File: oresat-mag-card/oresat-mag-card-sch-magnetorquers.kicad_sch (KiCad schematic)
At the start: 79 parts, among them U12 STSPIN250, U13 STSPIN250, U14 INA185, U15 INA185, U16 STSPIN250, U17 INA185

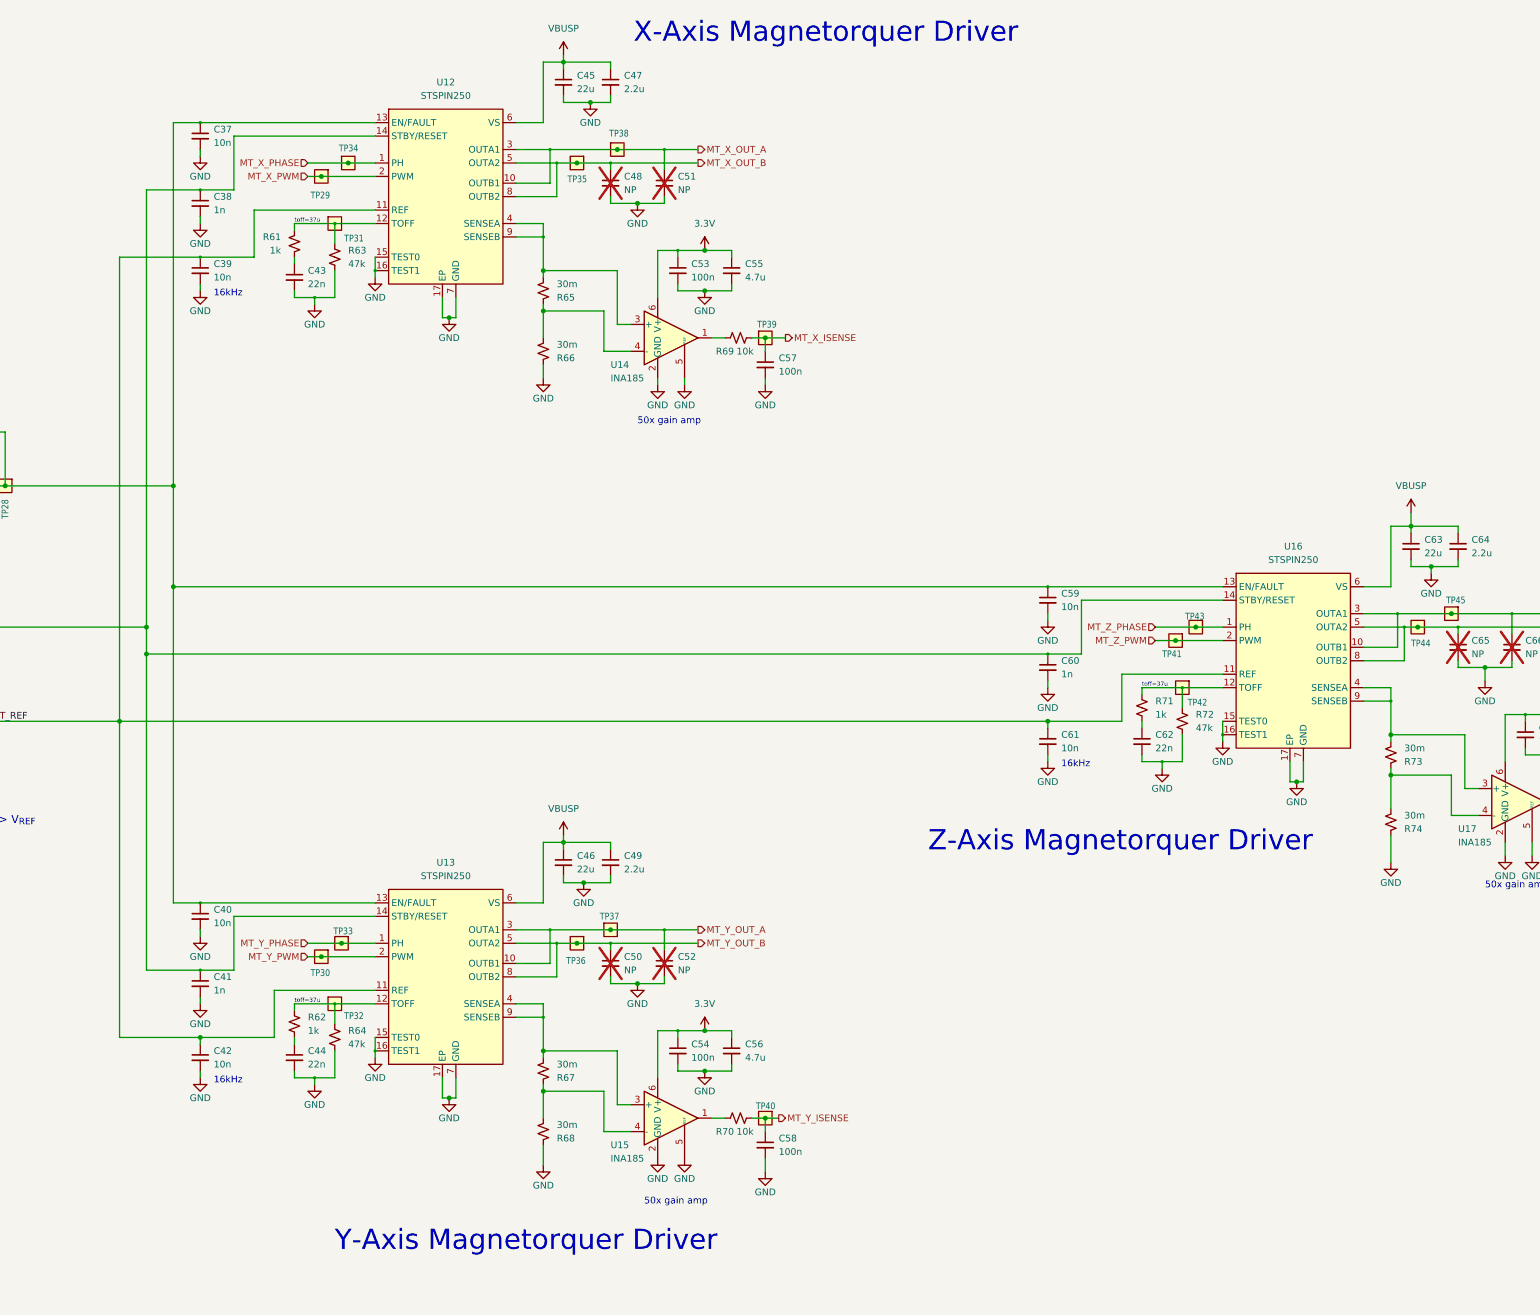
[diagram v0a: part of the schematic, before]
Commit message: Schematic polish, fixed UART TX/RX mixup, imported into layout
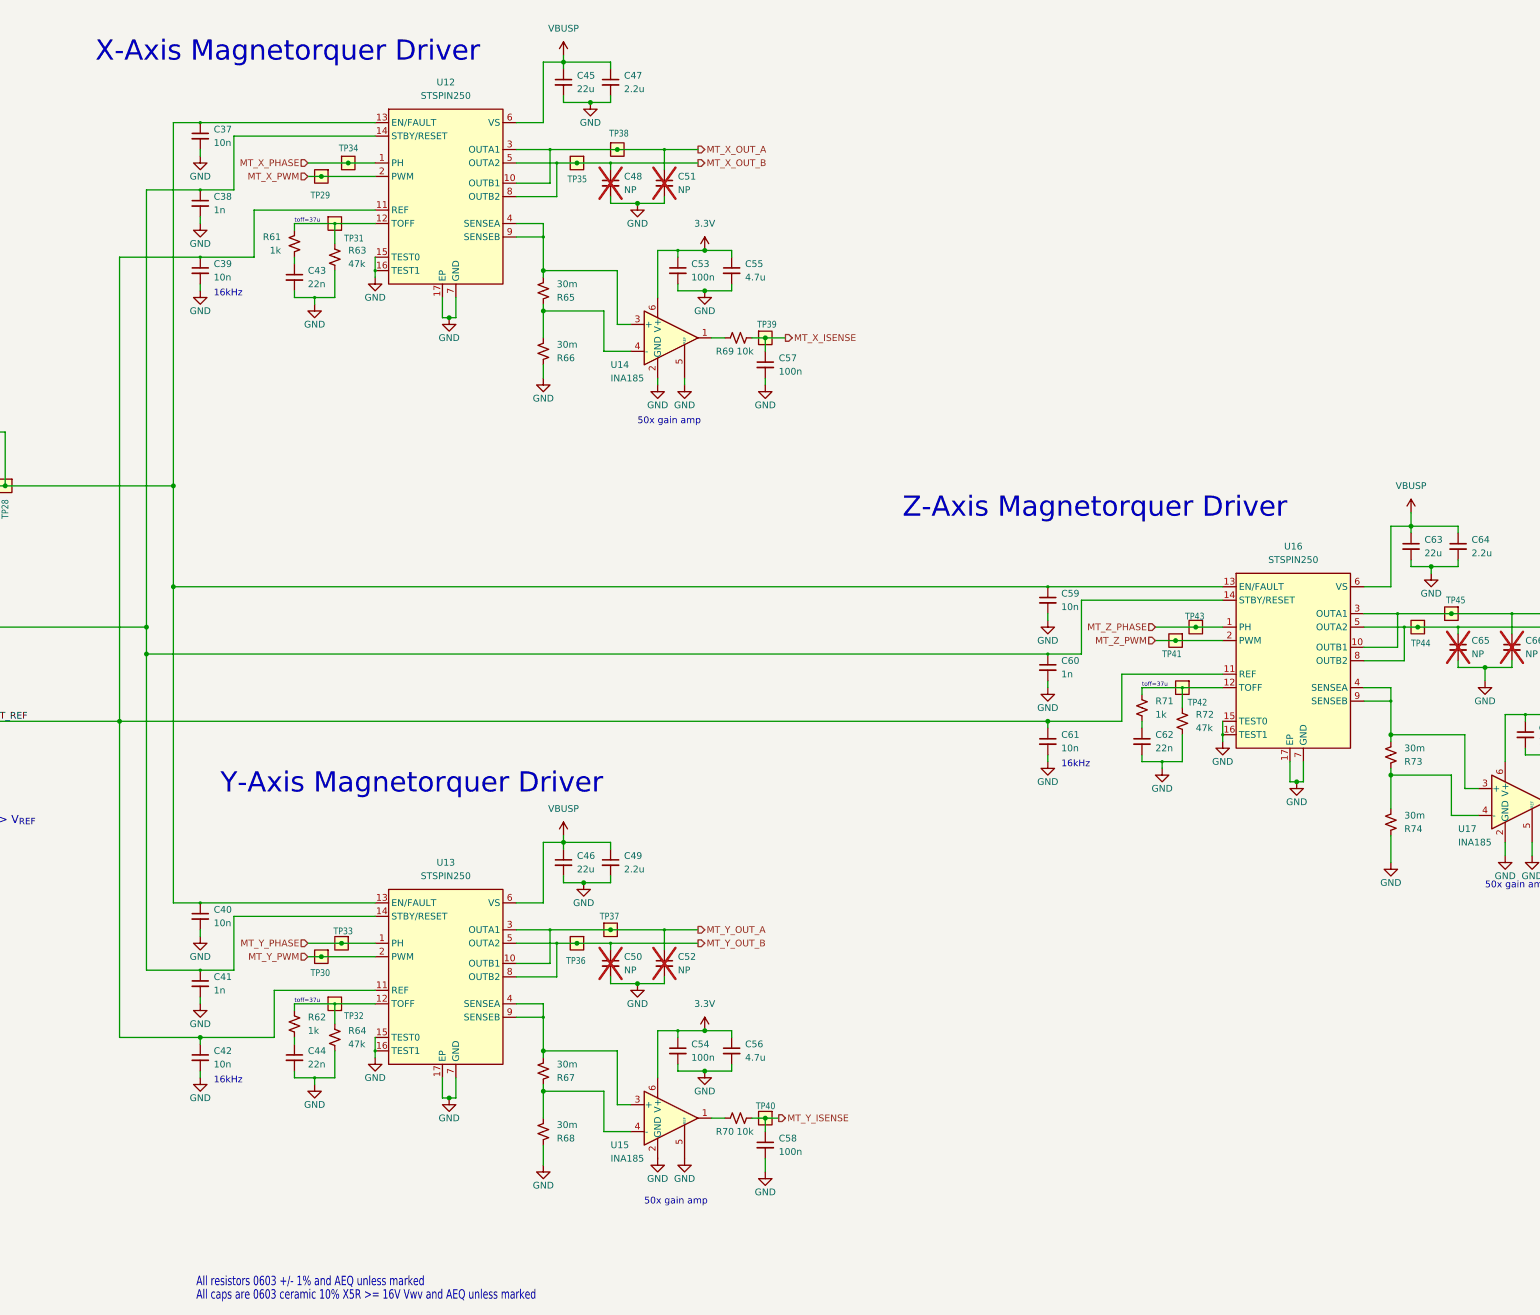
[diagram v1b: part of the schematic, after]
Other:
- note added: "All caps are 0603 ceramic 10% X5R >= 16V Vwv and AEQ unless marked"
- note added: "All resistors 0603 +/- 1% and AEQ unless marked"
- company: Edward Tsoi -> Portland State Aerospace Society
- title: Magnetorquers -> OreSat Mag Card

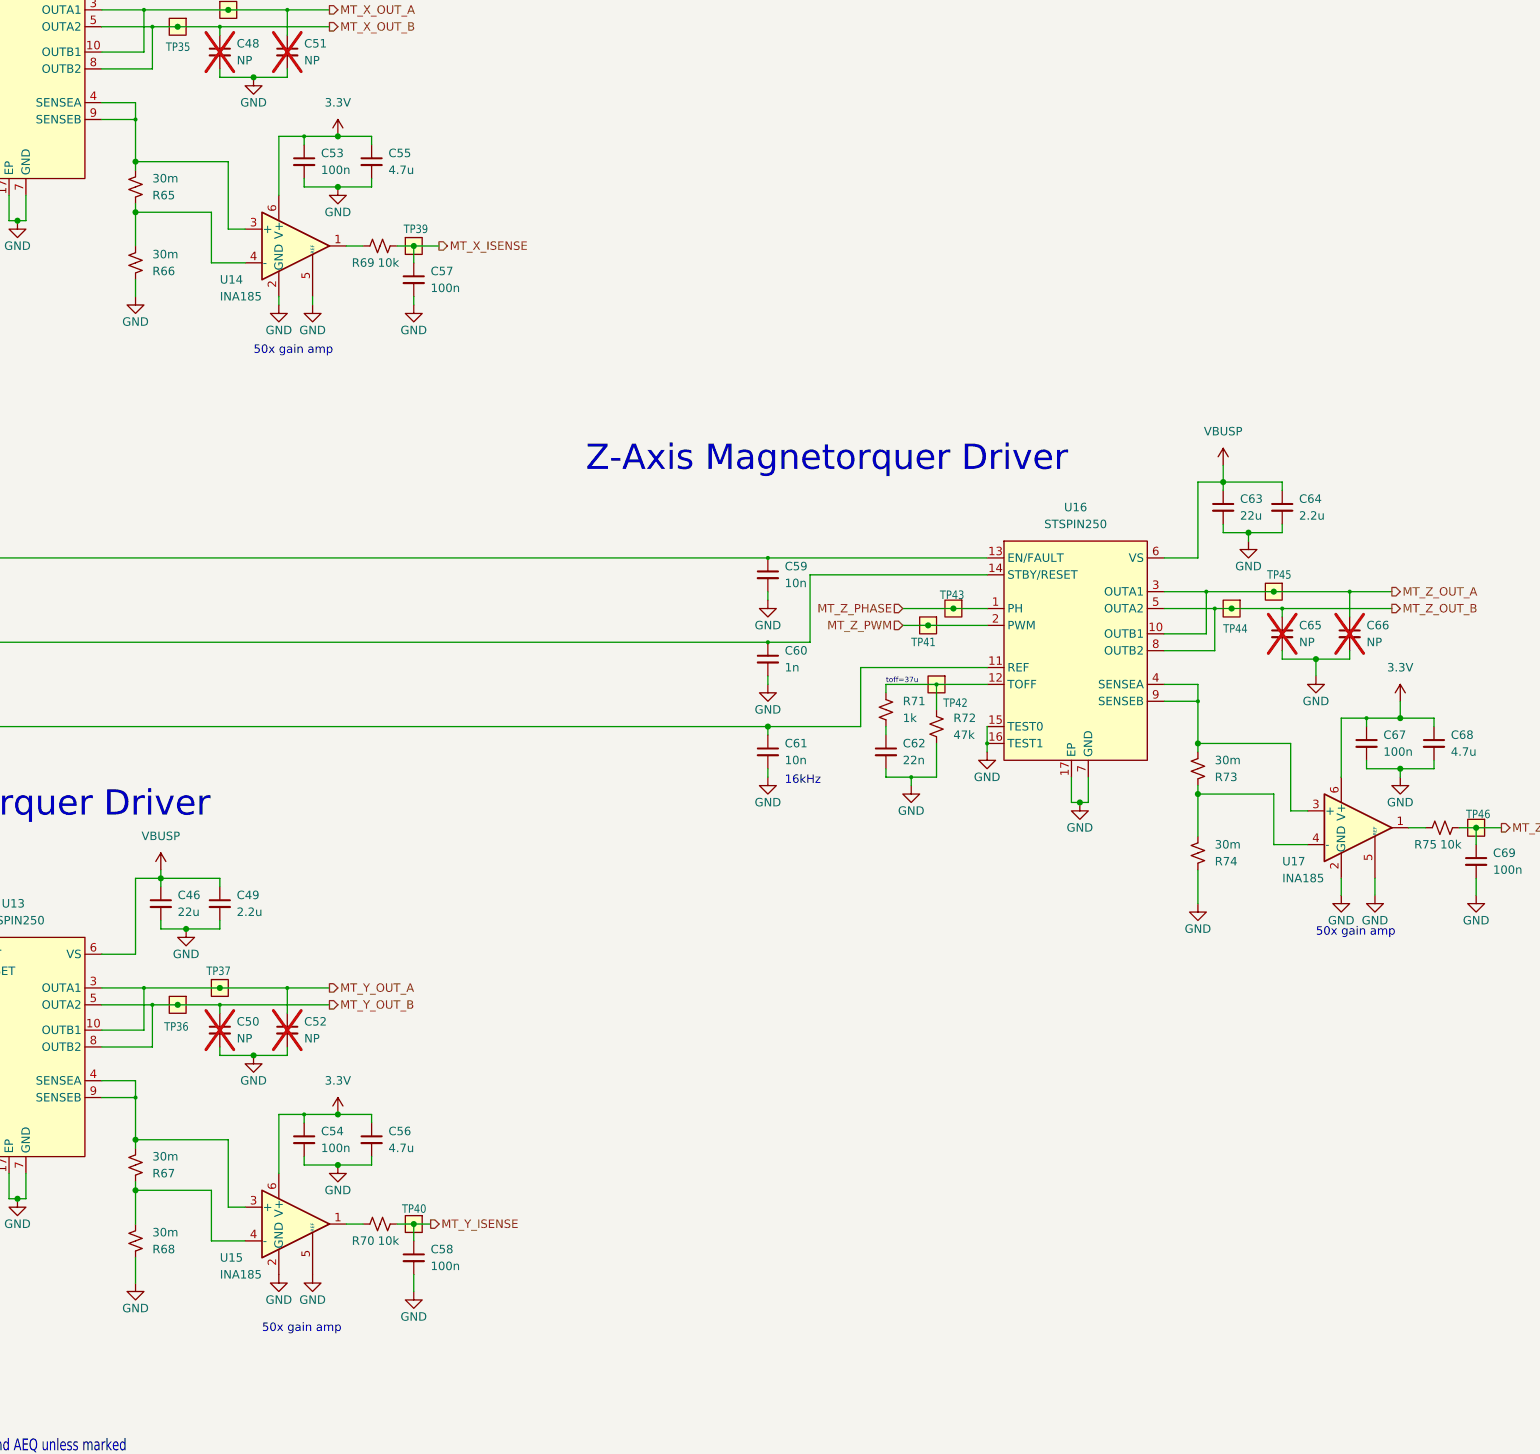
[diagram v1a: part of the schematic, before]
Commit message: No DRC errors
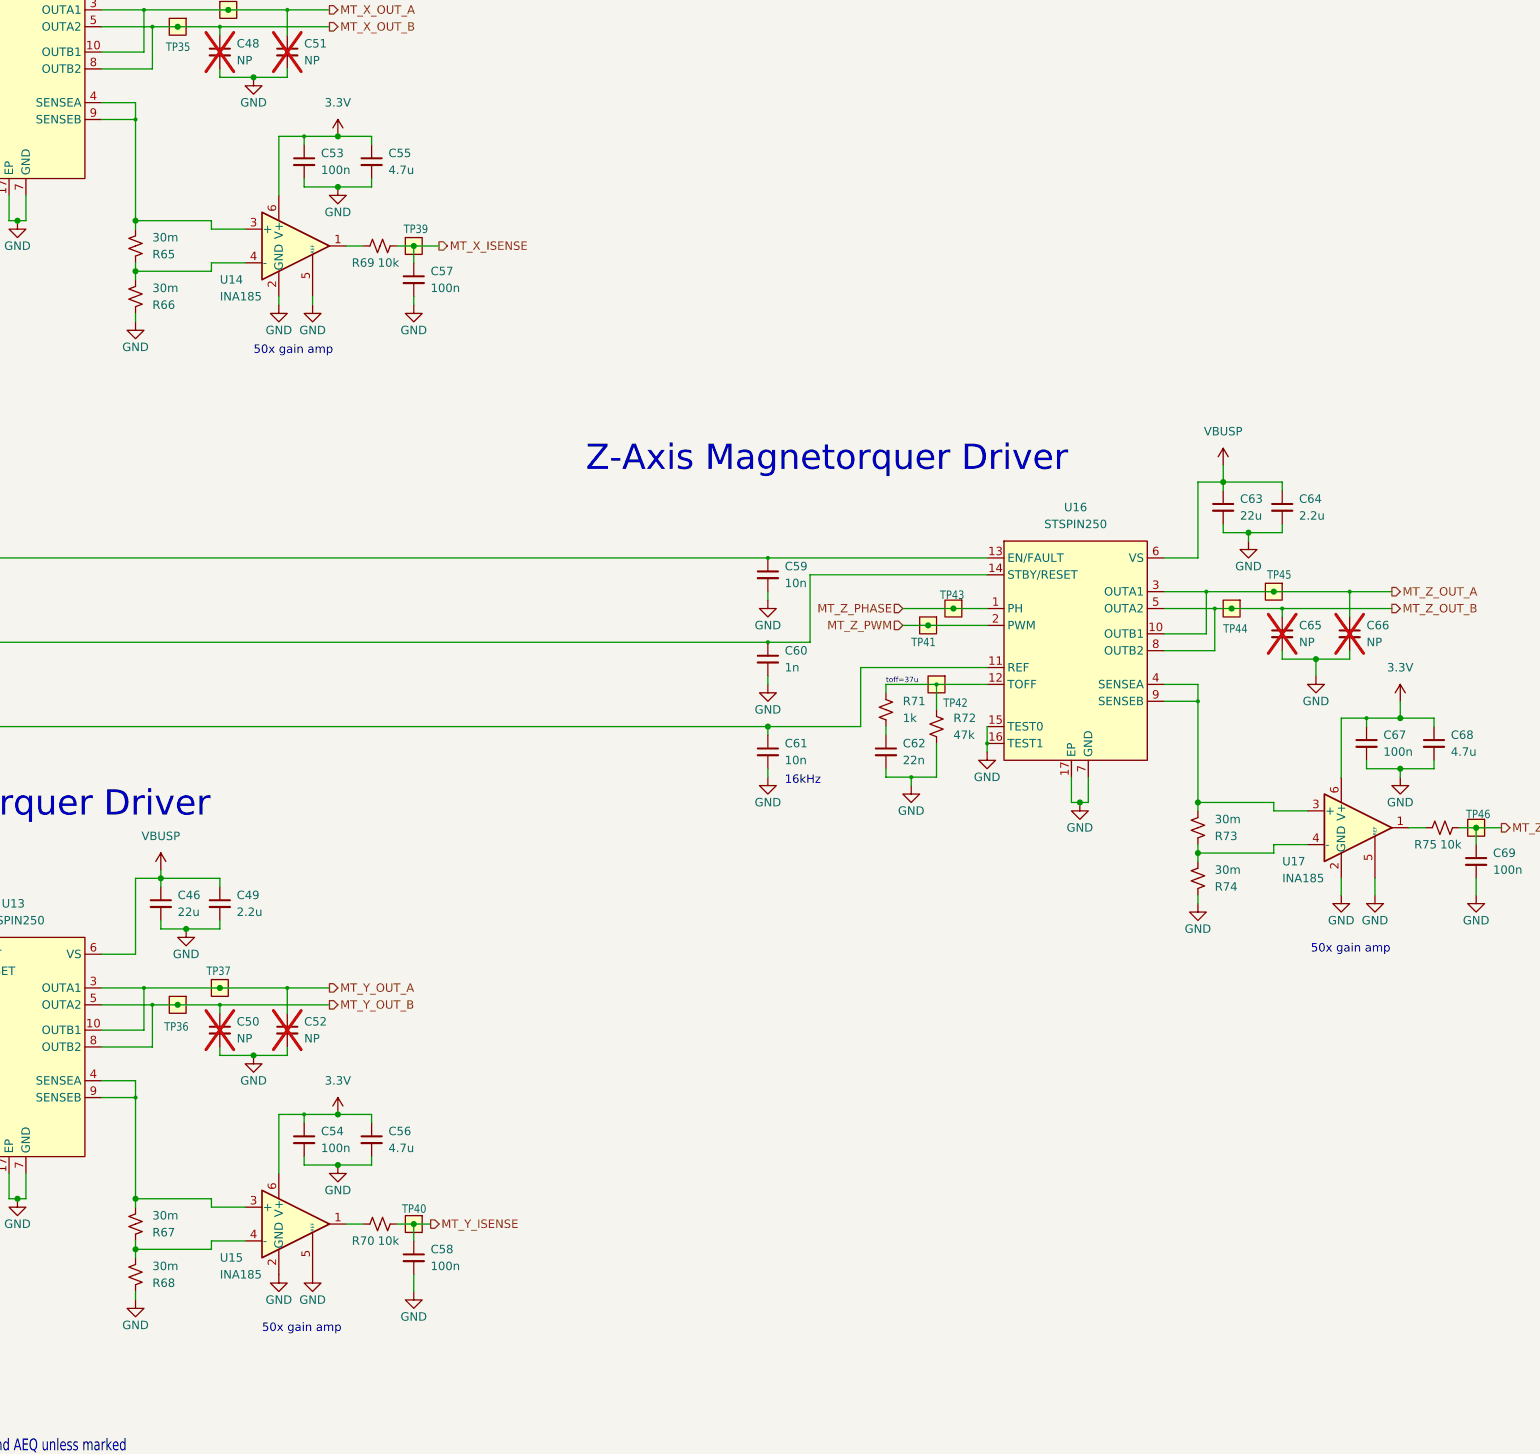
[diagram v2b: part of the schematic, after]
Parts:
- C37, C38, C39, C40, C41, C42, C43, C44, C47, C48, C49, C50, C51, C52, C53, C54, C55, C56, C57, C58, C59, C60, C61, C62, C64, C65, C66, C67, C68, C69, R58, R59, R60, R61, R62, R63, R64, R71, R72: footprint oresat-passives:c_0603-SMALL -> oresat-passives:0603-C-NOSILK
- R57, R69, R70, R75: footprint Resistor_SMD:R_0603_1608Metric -> oresat-passives:0603-C-NOSILK
- R65, R66, R67, R68, R73, R74: footprint Resistor_SMD:R_1206_3216Metric -> oresat-passives:1206-C
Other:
- moved on the sheet: R65, R66, R67, R68, R73, R74
